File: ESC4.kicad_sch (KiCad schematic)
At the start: 35 parts, among them J13 SWD1, J14 MOTOR1, Q10 XRS306D, Q11 XRS306D, Q12 XRS306D, U14 STM32G071GBUxN, U15 DRV8300D

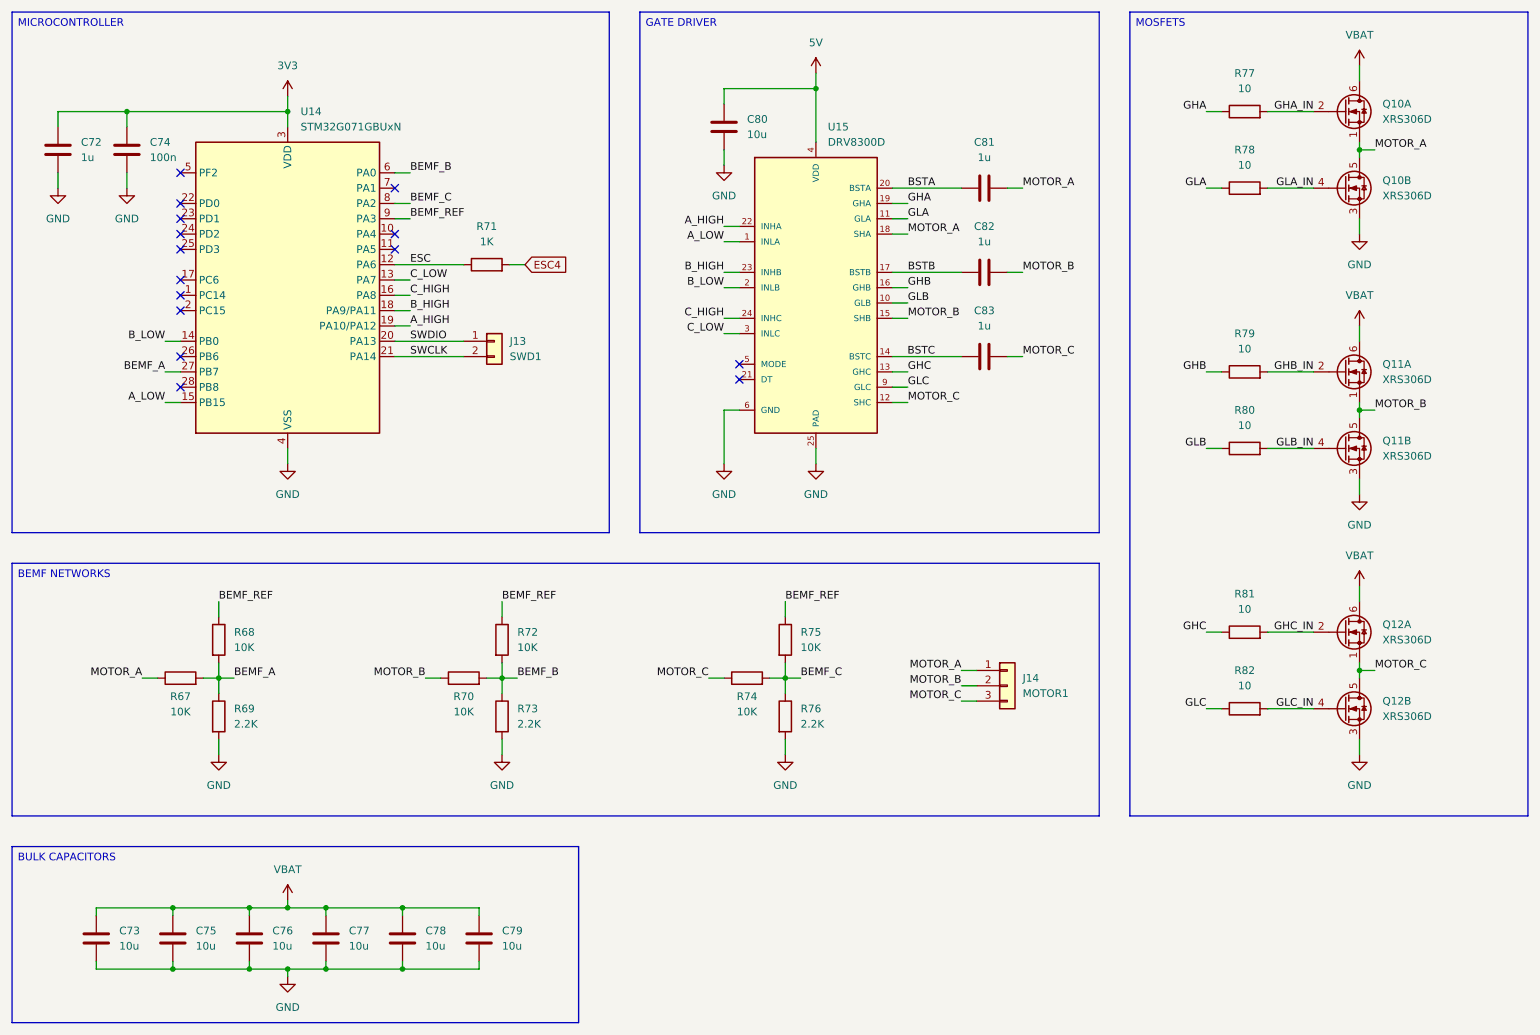
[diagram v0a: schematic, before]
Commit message: Schematic revision
Added an ESP32 C3 for the ELRS receiver.
Updated the protection approach for the board.
Updated the net nodes.
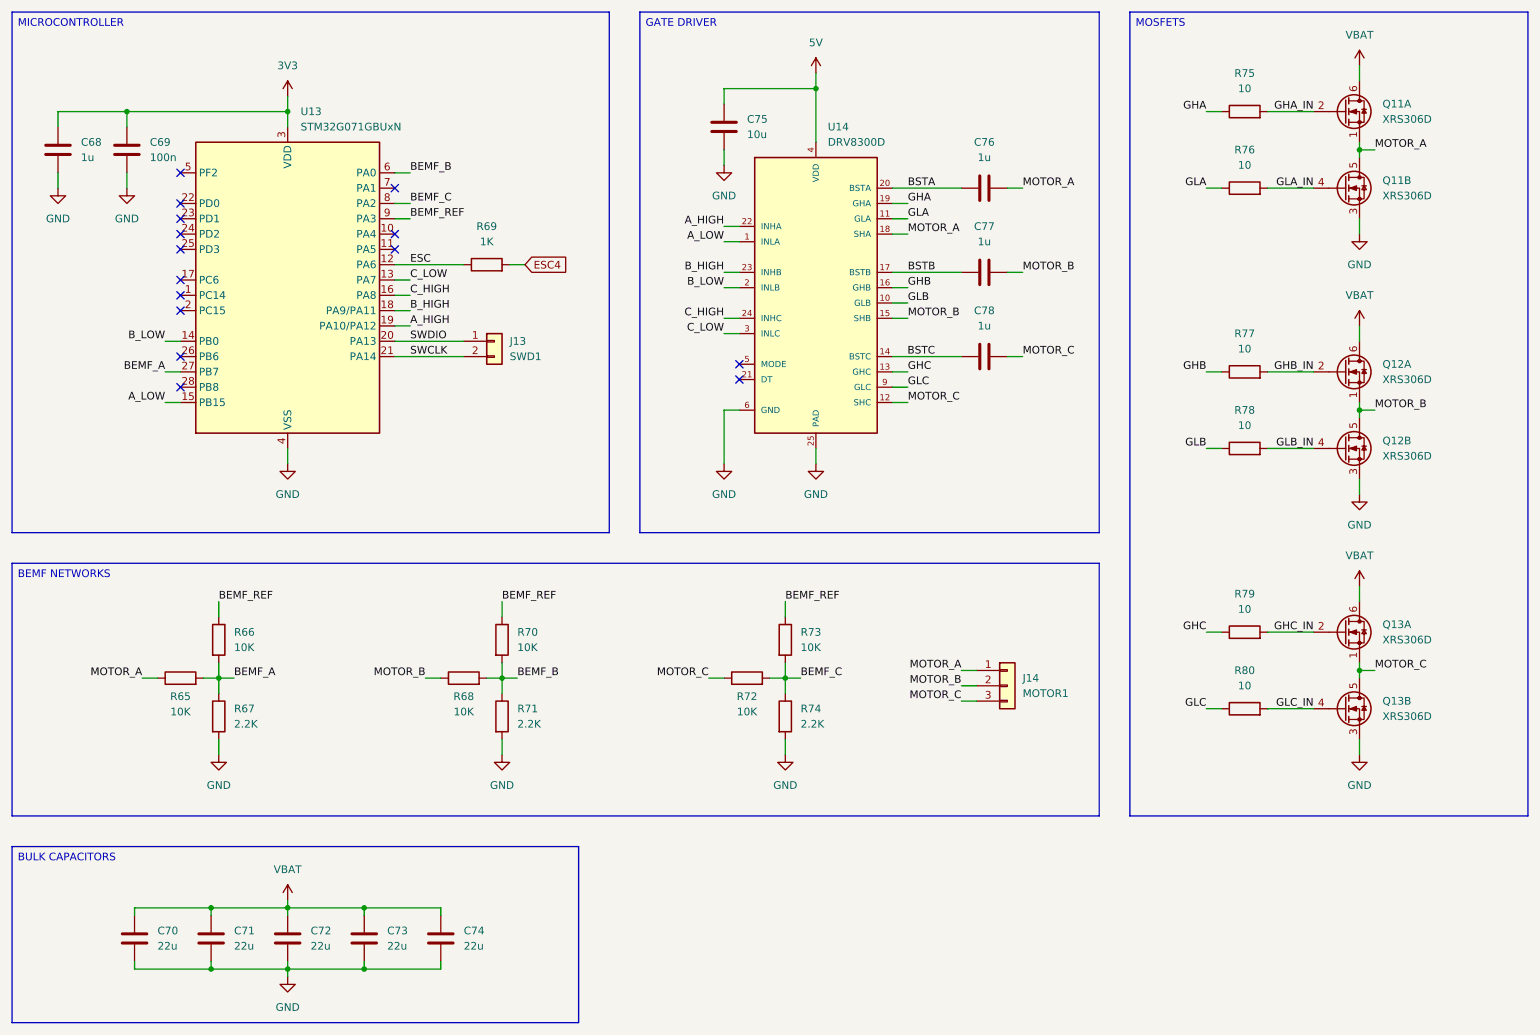
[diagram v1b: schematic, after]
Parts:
- removed C75, C76, C77, C78, C79: 10u, Capacitor_SMD:C_1206_3216Metric, symbol Device:C
- added C70, C71, C72, C74: 22u, Capacitor_SMD:C_1206_3216Metric, symbol Device:C
- C73: value 10u -> 22u
- renumbered C72 to C68, C74 to C69, C80 to C75, C81 to C76, C82 to C77, C83 to C78, Q10 to Q11, Q11 to Q12, Q12 to Q13, R67 to R65, R68 to R66, R69 to R67, R70 to R68, R71 to R69, R72 to R70, R73 to R71, R74 to R72, R75 to R73, R76 to R74, R77 to R75, R78 to R76, R79 to R77, R80 to R78, R81 to R79, R82 to R80, U14 to U13, U15 to U14
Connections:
- net GND: now also C70.2, C71.2, C72.2, C74.2
- net VBAT: now also C70.1, C71.1, C72.1, C74.1

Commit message: IMU filtering and layout
Added a missing capacitor for the IMU.
Updated the PCB layout.
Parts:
- renumbered C68 to C63, C69 to C64, C70 to C65, C71 to C66, C72 to C67, C73 to C68, C74 to C69, C75 to C70, C76 to C71, C77 to C72, C78 to C73

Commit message: Oscillator and IMU layout
Updated the oscillator layout for the RP2350.
Updated the IMU layout for the IMU.
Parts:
- renumbered C63 to C64, C64 to C65, C65 to C66, C66 to C67, C67 to C68, C68 to C69, C69 to C70, C70 to C71, C71 to C72, C72 to C73, C73 to C74
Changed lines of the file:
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@@
 		(dnp no)
 		(fields_autoplaced yes)
-		(property "Reference" "C63"
+		(property "Reference" "C64"
 			(at 34.29 44.4499 0)
 			(effects
@@
 			(project "ThunderHorse"
 				(path "/ac187c6c-fa53-41cc-bce1-6f39a42a92e8/807a5f6f-4255-4cf0-8d90-acd62bb18590/c0aa3042-c8c9-4ed2-b5c5-e577006d065c"
-					(reference "C63")
+					(reference "C64")
 					(unit 1)
 				)
@@
 		(dnp no)
 		(fields_autoplaced yes)
-		(property "Reference" "C66"
+		(property "Reference" "C67"
 			(at 59.69 175.2599 0)
 			(effects
@@
 			(project "ThunderHorse"
 				(path "/ac187c6c-fa53-41cc-bce1-6f39a42a92e8/807a5f6f-4255-4cf0-8d90-acd62bb18590/c0aa3042-c8c9-4ed2-b5c5-e577006d065c"
-					(reference "C66")
+					(reference "C67")
 					(unit 1)
 				)
@@
 		(dnp no)
 		(fields_autoplaced yes)
-		(property "Reference" "C67"
+		(property "Reference" "C68"
 			(at 72.39 175.2599 0)
 			(effects
@@
 			(project "ThunderHorse"
 				(path "/ac187c6c-fa53-41cc-bce1-6f39a42a92e8/807a5f6f-4255-4cf0-8d90-acd62bb18590/c0aa3042-c8c9-4ed2-b5c5-e577006d065c"
-					(reference "C67")
+					(reference "C68")
 					(unit 1)
 				)
@@
 		(dnp no)
 		(fields_autoplaced yes)
-		(property "Reference" "C72"
+		(property "Reference" "C73"
 			(at 184.15 58.42 90)
 			(effects
@@
 			(project "ThunderHorse"
 				(path "/ac187c6c-fa53-41cc-bce1-6f39a42a92e8/807a5f6f-4255-4cf0-8d90-acd62bb18590/c0aa3042-c8c9-4ed2-b5c5-e577006d065c"
-					(reference "C72")
+					(reference "C73")
 					(unit 1)
 				)
@@
 		(dnp no)
 		(fields_autoplaced yes)
-		(property "Reference" "C68"
+		(property "Reference" "C69"
 			(at 85.09 175.2599 0)
 			(effects
@@
 			(project "ThunderHorse"
 				(path "/ac187c6c-fa53-41cc-bce1-6f39a42a92e8/807a5f6f-4255-4cf0-8d90-acd62bb18590/c0aa3042-c8c9-4ed2-b5c5-e577006d065c"
-					(reference "C68")
+					(reference "C69")
 					(unit 1)
 				)
@@
 		(dnp no)
 		(fields_autoplaced yes)
-		(property "Reference" "C69"
+		(property "Reference" "C70"
 			(at 97.79 175.2599 0)
 			(effects
@@
 			(project "ThunderHorse"
 				(path "/ac187c6c-fa53-41cc-bce1-6f39a42a92e8/807a5f6f-4255-4cf0-8d90-acd62bb18590/c0aa3042-c8c9-4ed2-b5c5-e577006d065c"
-					(reference "C69")
+					(reference "C70")
 					(unit 1)
 				)
@@
 		(dnp no)
 		(fields_autoplaced yes)
-		(property "Reference" "C70"
+		(property "Reference" "C71"
 			(at 144.78 40.6399 0)
 			(effects
@@
 			(project "ThunderHorse"
 				(path "/ac187c6c-fa53-41cc-bce1-6f39a42a92e8/807a5f6f-4255-4cf0-8d90-acd62bb18590/c0aa3042-c8c9-4ed2-b5c5-e577006d065c"
-					(reference "C70")
+					(reference "C71")
 					(unit 1)
 				)
@@
 		(on_board yes)
 		(dnp no)
-		(property "Reference" "C65"
+		(property "Reference" "C66"
 			(at 46.99 175.2599 0)
 			(effects
@@
 			(project "ThunderHorse"
 				(path "/ac187c6c-fa53-41cc-bce1-6f39a42a92e8/807a5f6f-4255-4cf0-8d90-acd62bb18590/c0aa3042-c8c9-4ed2-b5c5-e577006d065c"
-					(reference "C65")
+					(reference "C66")
 					(unit 1)
 				)
@@
 		(dnp no)
 		(fields_autoplaced yes)
-		(property "Reference" "C73"
+		(property "Reference" "C74"
 			(at 184.15 72.39 90)
 			(effects
@@
 			(project "ThunderHorse"
 				(path "/ac187c6c-fa53-41cc-bce1-6f39a42a92e8/807a5f6f-4255-4cf0-8d90-acd62bb18590/c0aa3042-c8c9-4ed2-b5c5-e577006d065c"
-					(reference "C73")
+					(reference "C74")
 					(unit 1)
 				)
@@
 		(dnp no)
 		(fields_autoplaced yes)
-		(property "Reference" "C71"
+		(property "Reference" "C72"
 			(at 184.15 44.45 90)
 			(effects
@@
 			(project "ThunderHorse"
 				(path "/ac187c6c-fa53-41cc-bce1-6f39a42a92e8/807a5f6f-4255-4cf0-8d90-acd62bb18590/c0aa3042-c8c9-4ed2-b5c5-e577006d065c"
-					(reference "C71")
+					(reference "C72")
 					(unit 1)
 				)
@@
 		(dnp no)
 		(fields_autoplaced yes)
-		(property "Reference" "C64"
+		(property "Reference" "C65"
 			(at 45.72 44.4499 0)
 			(effects
@@
 			(project "ThunderHorse"
 				(path "/ac187c6c-fa53-41cc-bce1-6f39a42a92e8/807a5f6f-4255-4cf0-8d90-acd62bb18590/c0aa3042-c8c9-4ed2-b5c5-e577006d065c"
-					(reference "C64")
+					(reference "C65")
 					(unit 1)
 				)

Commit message: Power and ESC layout
Updated the power layout.
Updated the ESC layout.

TODO:
Improve track spacing for the ESC.
Complete the power connections.
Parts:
- C71: footprint Capacitor_SMD:C_0805_2012Metric -> Capacitor_SMD:C_0603_1608Metric
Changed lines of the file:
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@@
 			)
 		)
-		(property "Footprint" "Capacitor_SMD:C_0805_2012Metric"
+		(property "Footprint" "Capacitor_SMD:C_0603_1608Metric"
 			(at 141.9352 45.72 0)
 			(effects

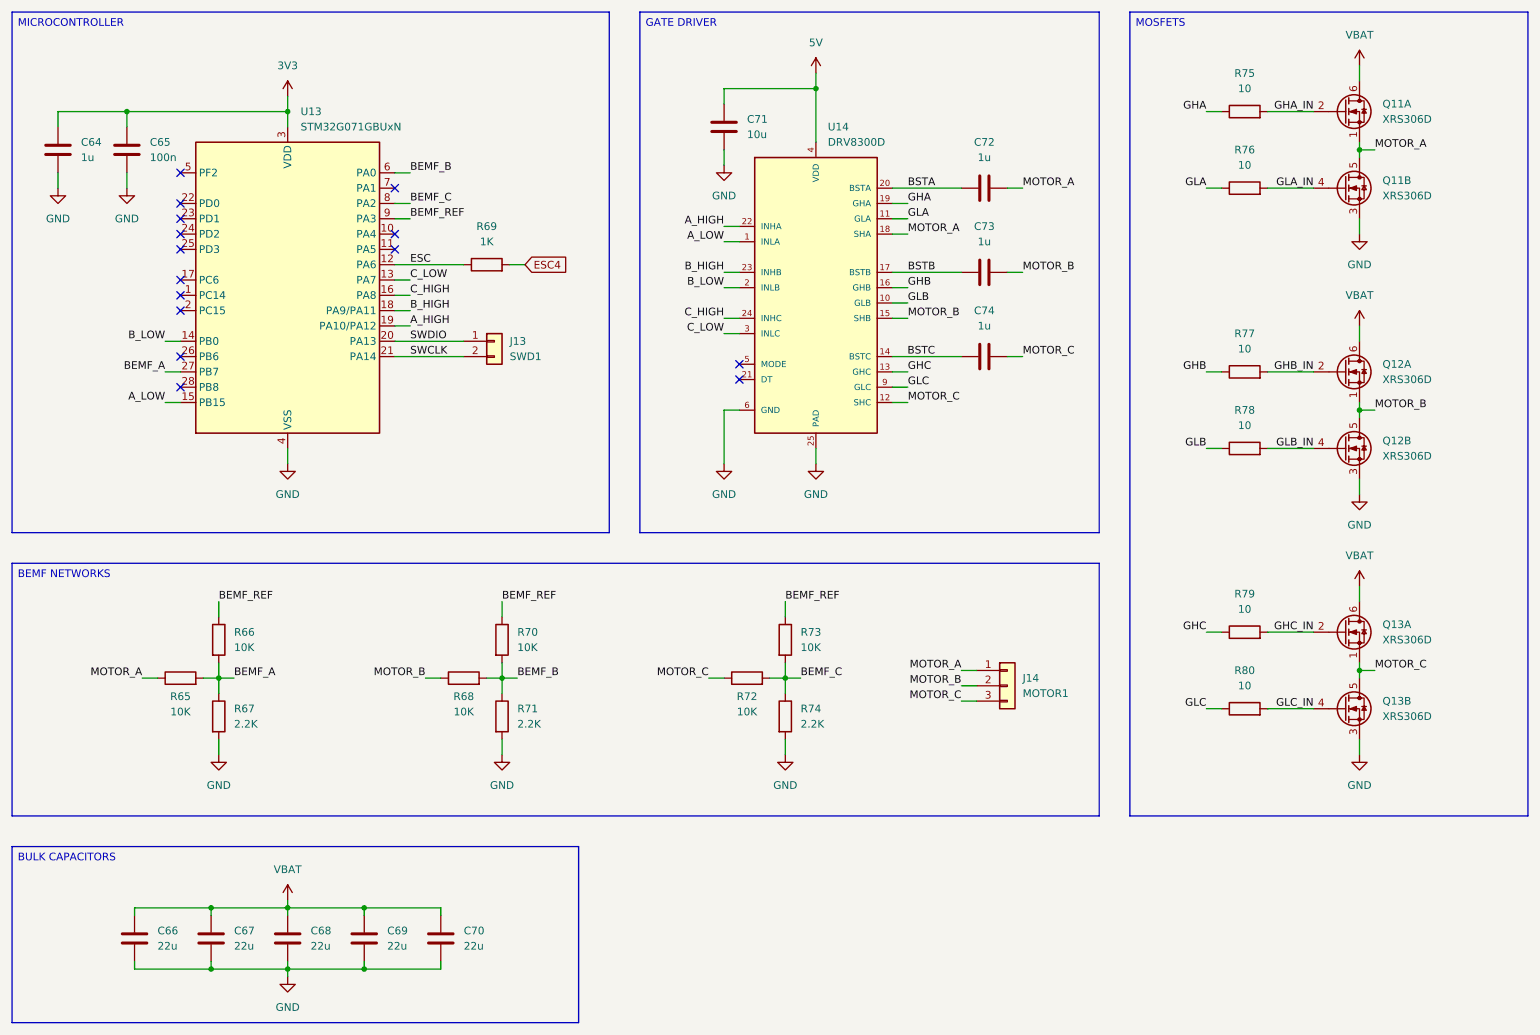
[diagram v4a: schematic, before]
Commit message: Voltage detection
Added a VBUS voltage detection for the RP.
Minor layout changes.
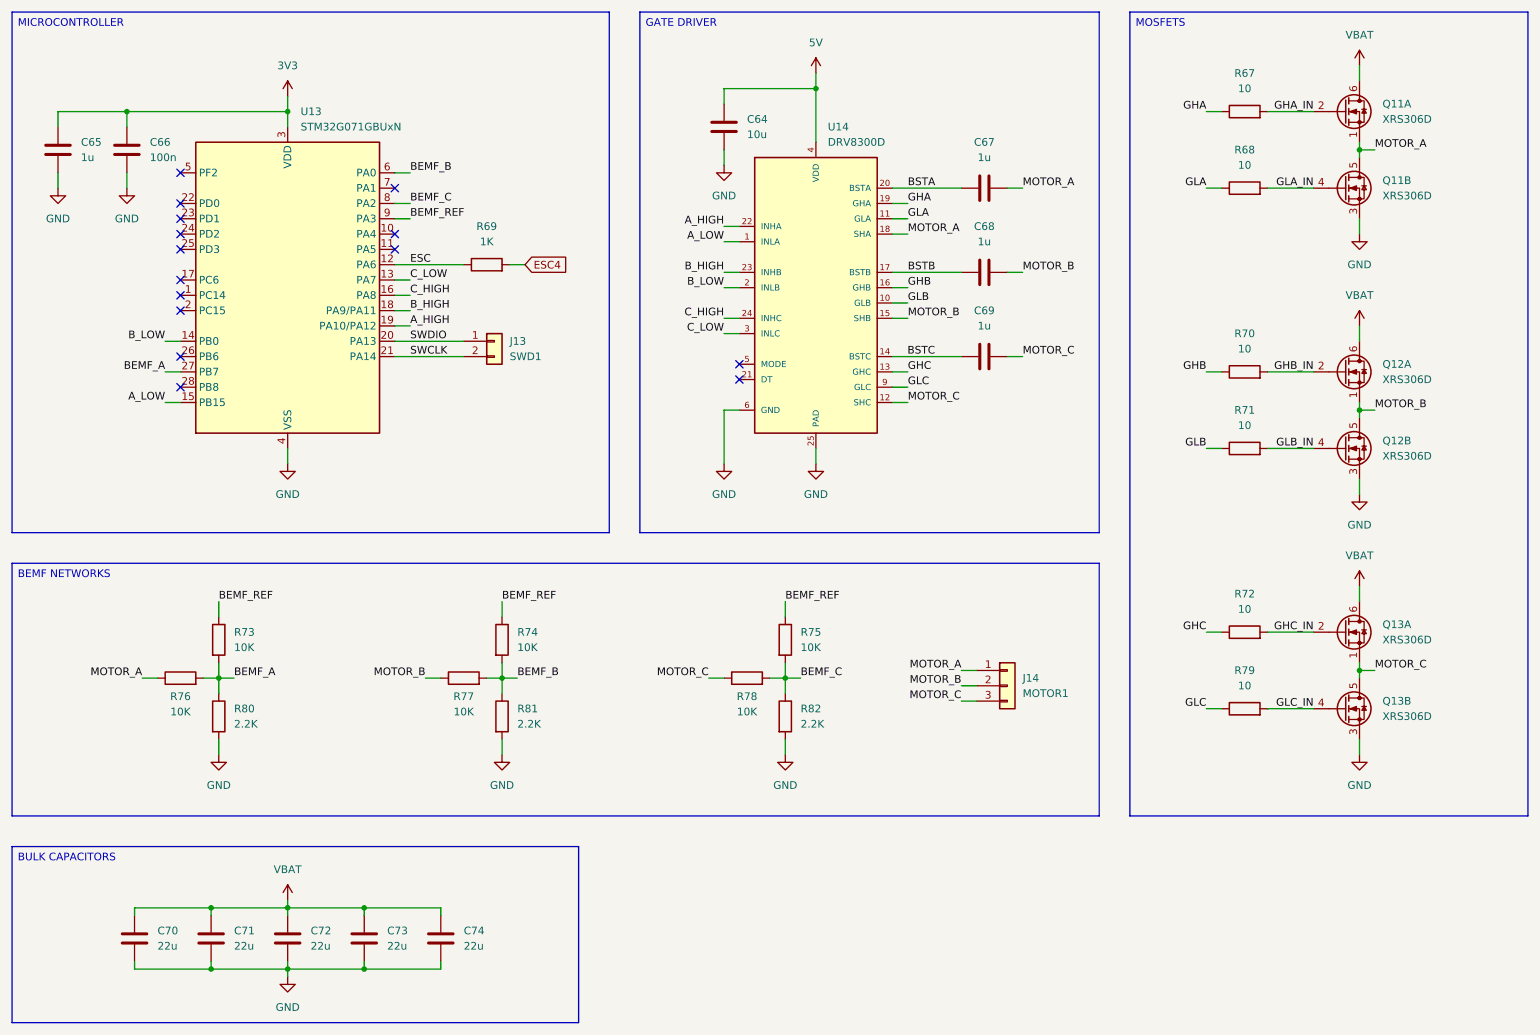
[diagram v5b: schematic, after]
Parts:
- renumbered C71 to C64, C64 to C65, C65 to C66, C72 to C67, C73 to C68, C74 to C69, C66 to C70, C67 to C71, C68 to C72, C69 to C73, C70 to C74, R75 to R67, R76 to R68, R77 to R70, R78 to R71, R79 to R72, R66 to R73, R70 to R74, R73 to R75, R65 to R76, R68 to R77, R72 to R78, R80 to R79, R67 to R80, R71 to R81, R74 to R82
